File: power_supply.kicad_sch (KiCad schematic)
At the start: 17 parts, among them U3 AP63203WU, U4 AP63205WU

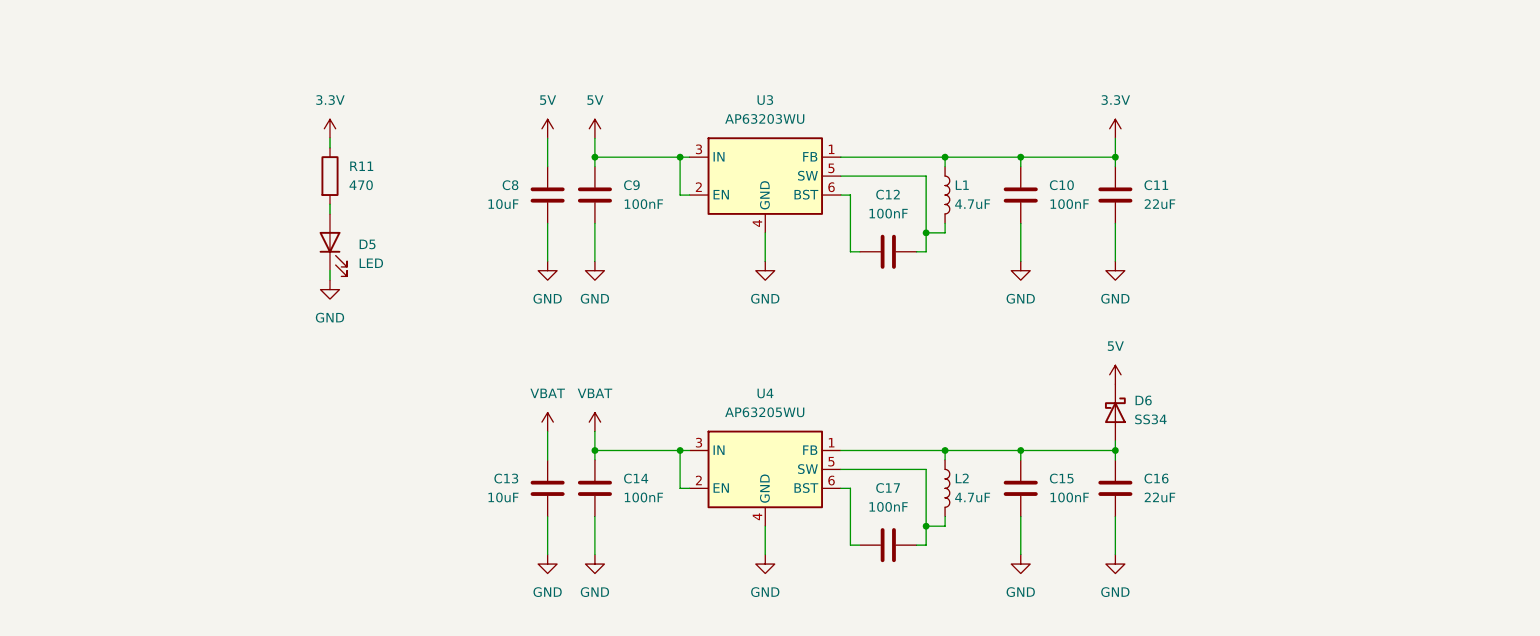
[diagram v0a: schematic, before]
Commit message: Replace schottky with ideal diode
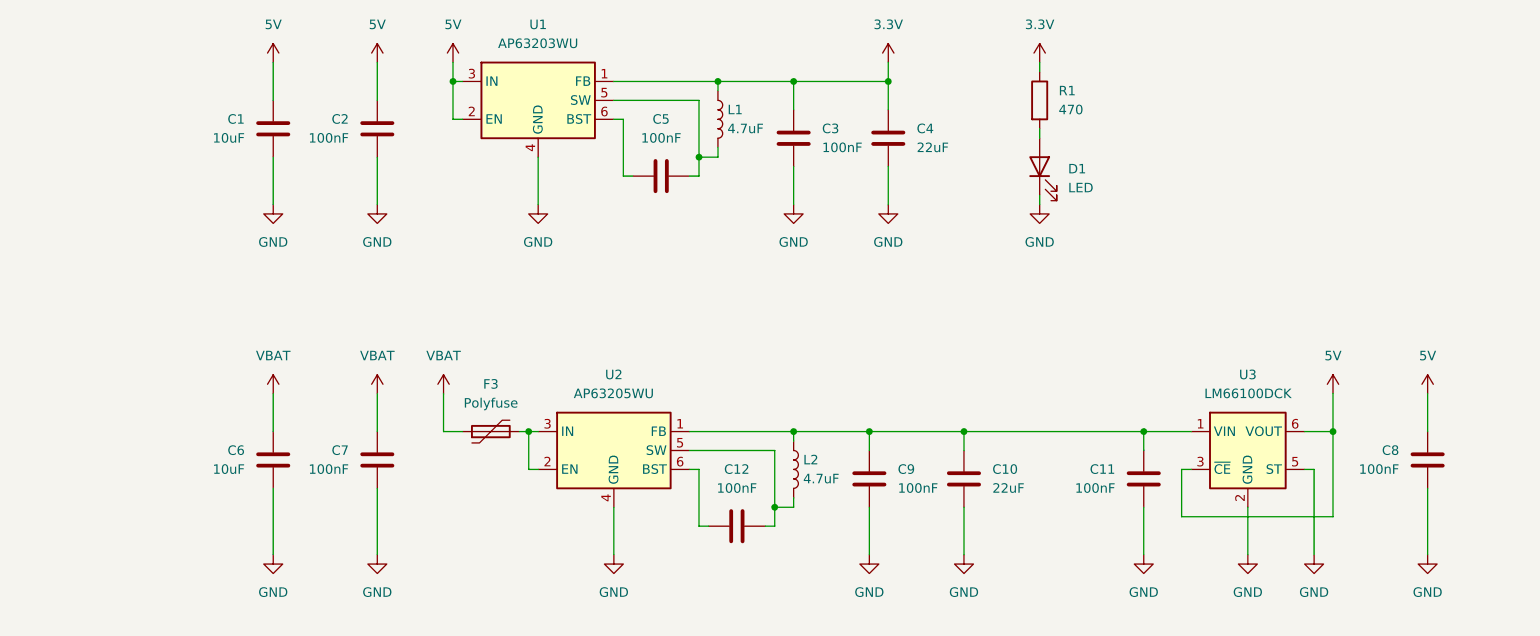
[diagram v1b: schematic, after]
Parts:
- removed D6: SS34, Diode_SMD:D_SMA, symbol Diode:SS34
- added C11, C8: 100nF, symbol Device:C
- added F3: Polyfuse, symbol Device:Polyfuse
- added U3: LM66100DCK, Package_TO_SOT_SMD:SOT-363_SC-70-6, symbol Power_Management:LM66100DCK
- renumbered C8 to C1, C16 to C10, C17 to C12, C9 to C2, C10 to C3, C11 to C4, C12 to C5, C13 to C6, C14 to C7, C15 to C9, D5 to D1, R11 to R1, U3 to U1, U4 to U2
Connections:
- net 5V: now also C8.1, U3.3 (~{CE}), U3.6 (VOUT)
- net GND: now also C11.2, C8.2, U3.2 (GND), U3.5 (ST)
- net VBAT: now also F3.1; no longer U2.2 (EN), U2.3 (IN)
- net at C10.1, C9.1, L2.1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: now also C11.1, U3.1 (VIN)
- new net: F3.2, U2.2 (EN), U2.3 (IN)
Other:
- moved on the sheet: C1, C10, C12, C2, C3, C4, C5, C6, C7, C9, D1, L1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

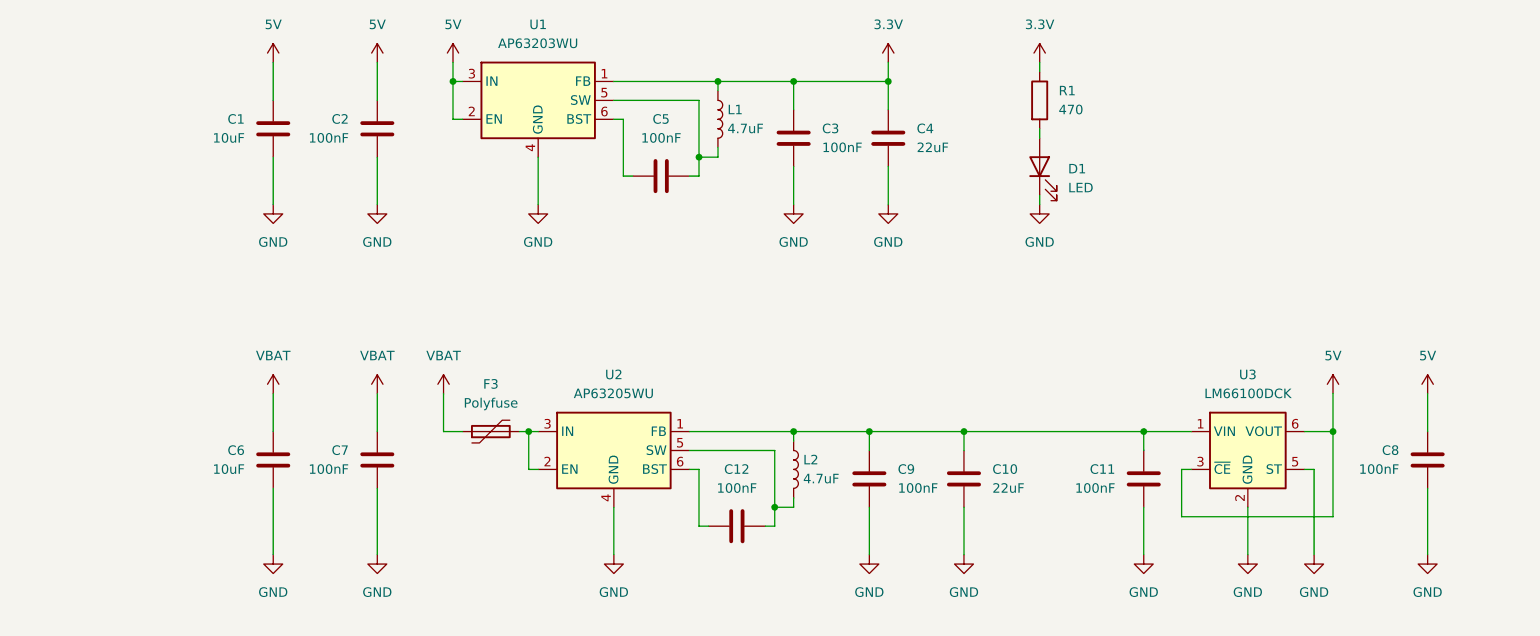
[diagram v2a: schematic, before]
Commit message: Follow DC-DC typical application
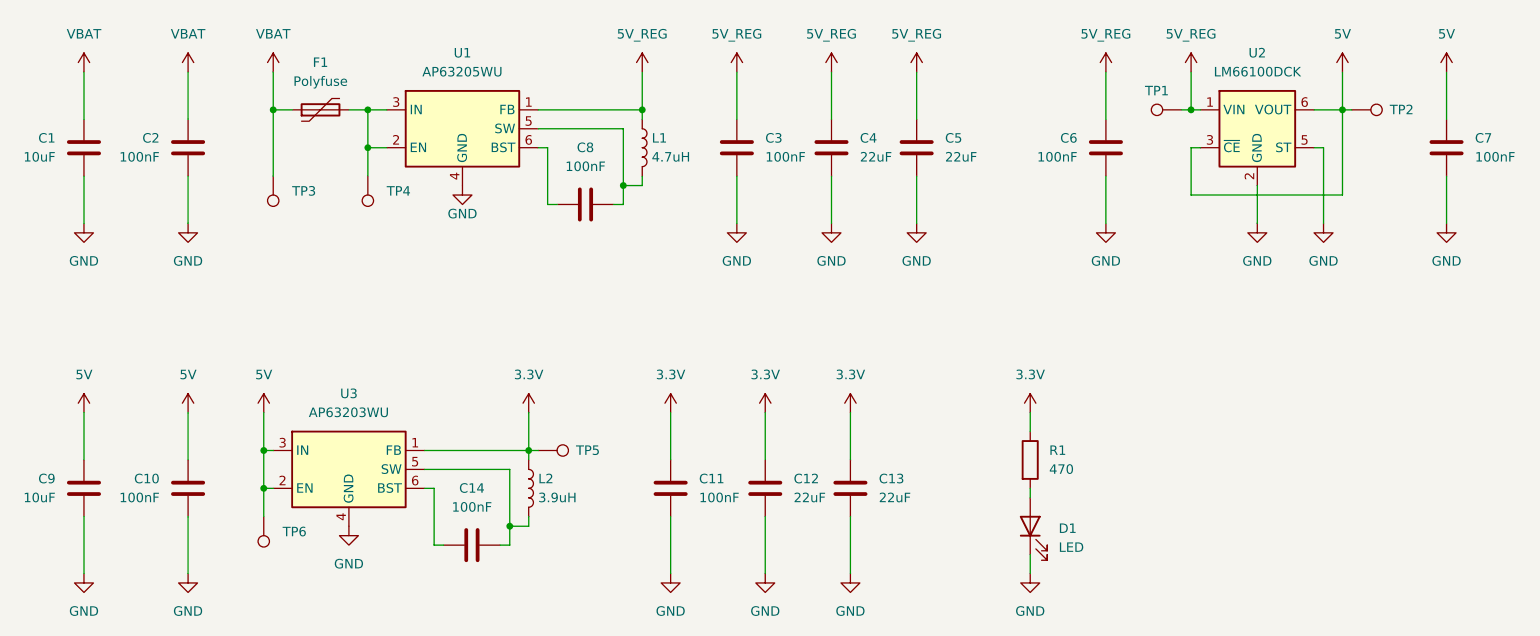
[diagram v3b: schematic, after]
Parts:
- added C13, C5: 22uF, symbol Device:C
- added TP1, TP2, TP3, TP4, TP5, TP6: TestPoint, symbol Connector:TestPoint
- L1: renamed from L2; value 4.7uF -> 4.7uH
- L2: renamed from L1; value 4.7uF -> 3.9uH
- renumbered C6 to C1, C2 to C10, C3 to C11, C4 to C12, C5 to C14, C7 to C2, C9 to C3, C10 to C4, C11 to C6, C8 to C7, C12 to C8, C1 to C9, F3 to F1, U2 to U1, U3 to U2, U1 to U3
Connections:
- net 3.3V: now also C13.1, TP5.1
- net 5V: now also TP2.1, TP6.1
- net GND: now also C13.2, C5.2
- net VBAT: now also TP3.1
- net 5V_REG: now reaches C3.1, C4.1, C6.1, L1.1, U1.1 (FB), U2.1 (VIN)
- net 5V_REG: now also C5.1, TP1.1
- net at F1.2, U1.2 (EN), U1.3 (IN): now also TP4.1
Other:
- moved on the sheet: C1, C10, C11, C12, C14, C2, C3, C4, C6, C7, C8, C9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

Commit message: Assign footprints
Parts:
- C1, C12, C13, C4, C5, C9: footprint (none) -> Capacitor_SMD:C_0603_1608Metric_Pad1.08x0.95mm_HandSolder
- C10, C11, C14, C2, C3, C6, C7, C8: footprint (none) -> Capacitor_SMD:C_0402_1005Metric_Pad0.74x0.62mm_HandSolder
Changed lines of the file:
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@@
 			)
 		)
-		(property "Footprint" ""
+		(property "Footprint" "Capacitor_SMD:C_0402_1005Metric_Pad0.74x0.62mm_HandSolder"
 			(at 106.68 127.9652 0)
 			(effects
@@
 			)
 		)
-		(property "Footprint" ""
+		(property "Footprint" "Capacitor_SMD:C_0603_1608Metric_Pad1.08x0.95mm_HandSolder"
 			(at 57.4548 123.19 0)
 			(effects
@@
 			)
 		)
-		(property "Footprint" ""
+		(property "Footprint" "Capacitor_SMD:C_0402_1005Metric_Pad0.74x0.62mm_HandSolder"
 			(at 242.2652 77.47 0)
 			(effects
@@
 			)
 		)
-		(property "Footprint" ""
+		(property "Footprint" "Capacitor_SMD:C_0603_1608Metric_Pad1.08x0.95mm_HandSolder"
 			(at 162.2552 123.19 0)
 			(effects
@@
 			)
 		)
-		(property "Footprint" ""
+		(property "Footprint" "Capacitor_SMD:C_0603_1608Metric_Pad1.08x0.95mm_HandSolder"
 			(at 57.4548 77.47 0)
 			(effects
@@
 			)
 		)
-		(property "Footprint" ""
+		(property "Footprint" "Capacitor_SMD:C_0402_1005Metric_Pad0.74x0.62mm_HandSolder"
 			(at 147.0152 77.47 0)
 			(effects
@@
 			)
 		)
-		(property "Footprint" ""
+		(property "Footprint" "Capacitor_SMD:C_0603_1608Metric_Pad1.08x0.95mm_HandSolder"
 			(at 171.1452 77.47 0)
 			(effects
@@
 			)
 		)
-		(property "Footprint" ""
+		(property "Footprint" "Capacitor_SMD:C_0603_1608Metric_Pad1.08x0.95mm_HandSolder"
 			(at 150.8252 123.19 0)
 			(effects
@@
 			)
 		)
-		(property "Footprint" ""
+		(property "Footprint" "Capacitor_SMD:C_0402_1005Metric_Pad0.74x0.62mm_HandSolder"
 			(at 194.6148 77.47 0)
 			(effects
@@
 			)
 		)
-		(property "Footprint" ""
+		(property "Footprint" "Capacitor_SMD:C_0402_1005Metric_Pad0.74x0.62mm_HandSolder"
 			(at 138.1252 123.19 0)
 			(effects
@@
 			)
 		)
-		(property "Footprint" ""
+		(property "Footprint" "Capacitor_SMD:C_0603_1608Metric_Pad1.08x0.95mm_HandSolder"
 			(at 159.7152 77.47 0)
 			(effects
@@
 			)
 		)
-		(property "Footprint" ""
+		(property "Footprint" "Capacitor_SMD:C_0402_1005Metric_Pad0.74x0.62mm_HandSolder"
 			(at 121.92 82.2452 0)
 			(effects
@@
 			)
 		)
-		(property "Footprint" ""
+		(property "Footprint" "Capacitor_SMD:C_0402_1005Metric_Pad0.74x0.62mm_HandSolder"
 			(at 71.4248 123.19 0)
 			(effects
@@
 			)
 		)
-		(property "Footprint" ""
+		(property "Footprint" "Capacitor_SMD:C_0402_1005Metric_Pad0.74x0.62mm_HandSolder"
 			(at 71.4248 77.47 0)
 			(effects

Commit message: Update LCSC symbol field
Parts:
- U2: LCSC Part (none) -> C2869734; LSCS Part No. C2869734 -> (none)
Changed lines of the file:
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@@
 			)
 		)
-		(property "LSCS Part No." "C2869734"
+		(property "LCSC Part" "C2869734"
 			(at 215.9 71.12 0)
 			(effects

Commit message: Assign LCSC part numbers
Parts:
- U1: LCSC Part (none) -> C2071056
- U3: LCSC Part (none) -> C780769
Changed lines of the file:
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@@
+			)
+		)
+		(property "LCSC Part" "C2071056"
+			(at 109.22 71.12 0)
+			(effects
+				(font
+					(size 1.27 1.27)
+				)
+				(hide yes)
 			)
 		)
@@
 			(at 93.98 116.84 0)
 			(effects
+				(font
+					(size 1.27 1.27)
+				)
+				(hide yes)
+			)
+		)
+		(property "LCSC Part" "C780769"
+			(at 93.98 116.84 0)
+			(effects
